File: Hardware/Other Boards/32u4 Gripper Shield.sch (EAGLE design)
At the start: 22 parts, among them Q1 MOSFET-NCHANNELSMD, Q2 MOSFET-NCHANNELSMD, U1 SN74LS241DW, U2 XBEE-1B3, U3 V_REG_LDOSMD

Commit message: Few more things with shield
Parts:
- Q1, Q2: value MOSFET-NCHANNELSMD -> MOSFET-NCHANNELBSS138; device SparkFun-DiscreteSemi:MOSFET-NCHANNELSMD -> SparkFun-DiscreteSemi:MOSFET-NCHANNELBSS138
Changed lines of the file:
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@@
 <part name="P+3" library="SparkFun" deviceset="3.3V" device=""/>
 <part name="P+4" library="SparkFun" deviceset="3.3V" device=""/>
-<part name="Q1" library="SparkFun-DiscreteSemi" deviceset="MOSFET-NCHANNEL" device="SMD"/>
+<part name="Q1" library="SparkFun-DiscreteSemi" deviceset="MOSFET-NCHANNEL" device="BSS138"/>
 <part name="R5" library="SparkFun-Passives" deviceset="RESISTOR" device="1206" value="1k"/>
 <part name="R6" library="SparkFun-Passives" deviceset="RESISTOR" device="1206" value="1k"/>
 <part name="P+5" library="SparkFun" deviceset="3.3V" device=""/>
 <part name="U$6" library="SparkFun" deviceset="5V" device=""/>
-<part name="Q2" library="SparkFun-DiscreteSemi" deviceset="MOSFET-NCHANNEL" device="SMD"/>
+<part name="Q2" library="SparkFun-DiscreteSemi" deviceset="MOSFET-NCHANNEL" device="BSS138"/>
 <part name="R7" library="SparkFun-Passives" deviceset="RESISTOR" device="1206" value="1k"/>
 <part name="R8" library="SparkFun-Passives" deviceset="RESISTOR" device="1206" value="1k"/>
@@
 <pinref part="JP1" gate="G$1" pin="3"/>
 <wire x1="63.5" y1="106.68" x2="73.66" y2="106.68" width="0.1524" layer="91"/>
+<label x="73.66" y="106.68" size="1.778" layer="95"/>
 </segment>
 <segment>
@@
 <pinref part="U$5" gate="G$1" pin="OUT"/>
 <wire x1="167.64" y1="142.24" x2="172.72" y2="142.24" width="0.1524" layer="91"/>
+<label x="172.72" y="142.24" size="1.778" layer="95" xref="yes"/>
 </segment>
 </net>
@@
 <pinref part="JP1" gate="G$1" pin="1"/>
 <wire x1="63.5" y1="101.6" x2="73.66" y2="101.6" width="0.1524" layer="91"/>
+<label x="73.66" y="101.6" size="1.778" layer="95"/>
 </segment>
 </net>
@@
 <pinref part="U$1" gate="G$1" pin="D3~"/>
 <wire x1="5.08" y1="55.88" x2="-2.54" y2="55.88" width="0.1524" layer="91"/>
+<label x="-5.08" y="55.88" size="1.778" layer="95"/>
 </segment>
 </net>
@@
 <pinref part="U$1" gate="G$1" pin="D2"/>
 <wire x1="5.08" y1="60.96" x2="-2.54" y2="60.96" width="0.1524" layer="91"/>
+<label x="-5.08" y="60.96" size="1.778" layer="95"/>
 </segment>
 </net>
@@
 <pinref part="JP1" gate="G$1" pin="2"/>
 <wire x1="63.5" y1="104.14" x2="73.66" y2="104.14" width="0.1524" layer="91"/>
+<label x="73.66" y="104.14" size="1.778" layer="95"/>
 </segment>
 <segment>
 <pinref part="U$5" gate="G$1" pin="IN"/>
 <wire x1="152.4" y1="142.24" x2="147.32" y2="142.24" width="0.1524" layer="91"/>
+<label x="147.32" y="142.24" size="1.778" layer="95" rot="R180" xref="yes"/>
 </segment>
 <segment>
 <pinref part="U$3" gate="G$1" pin="L"/>
 <wire x1="154.94" y1="162.56" x2="149.86" y2="162.56" width="0.1524" layer="91"/>
+<label x="149.86" y="162.56" size="1.778" layer="95" rot="R180" xref="yes"/>
 </segment>
 </net>
@@
 <pinref part="U$1" gate="G$1" pin="D1/TX"/>
 <wire x1="5.08" y1="71.12" x2="-2.54" y2="71.12" width="0.1524" layer="91"/>
+<label x="-5.08" y="71.12" size="1.778" layer="95"/>
 </segment>
 <segment>
@@
 <pinref part="U$1" gate="G$1" pin="D0/RX"/>
 <wire x1="5.08" y1="66.04" x2="-2.54" y2="66.04" width="0.1524" layer="91"/>
-</segment>
-<segment>
+<label x="-5.08" y="66.04" size="1.778" layer="95"/>
+</segment>
+<segment>

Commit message: Finished gripper shield
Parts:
- removed C1, C3: 10uF, SparkFun:CAP_POL1206
- removed C2: 0.1uF, SparkFun-Passives:CAP1206
- removed Q1, Q2: MOSFET-NCHANNELBSS138, SparkFun-DiscreteSemi:MOSFET-NCHANNELBSS138
- removed R5, R6, R7, R8: 1k, SparkFun-Passives:RESISTOR1206
- removed U3: V_REG_LDOSMD, SparkFun:V_REG_LDOSMD
- added S1, S2, S3, S4: STANDOFF_ELECTRICAL, SparkFun-Electromechanical:STANDOFF_ELECTRICAL
- U$3: value H_WR-TBL_3210002HORIZ -> H_WR-TBL_321*0002VERT; device MRDT-2015-PowerBoard:H_WR-TBL_3210002HORIZ -> MRDT-2015-PowerBoard:H_WR-TBL_3210002VERT
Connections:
- removed net 5V: C3.+, R6.2, R8.2, U$1.VCC, U$5.OUT, U1.VCC, U3.EN, U3.IN
- removed net DIN: Q1.D, R6.1
- removed net DOUT: Q2.D, R8.1
- net 3.3V: now also U$1.VCC, U$5.OUT, U1.VCC; no longer C1.+, C2.1, Q1.G, Q2.G, R5.2, R7.2, U3.OUT
- net DC_1: now also U$1.D4/A6
- net GND: now also S1.P$1, S2.P$1, S3.P$1, S4.P$1; no longer C1.-, C2.2, C3.-, U3.GND
- net RX_0: no longer Q2.S, R7.1
- net TX_0: no longer Q1.S, R5.1
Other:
- note removed: "500mA peak"
- note removed: "MIC5219-3.3V"

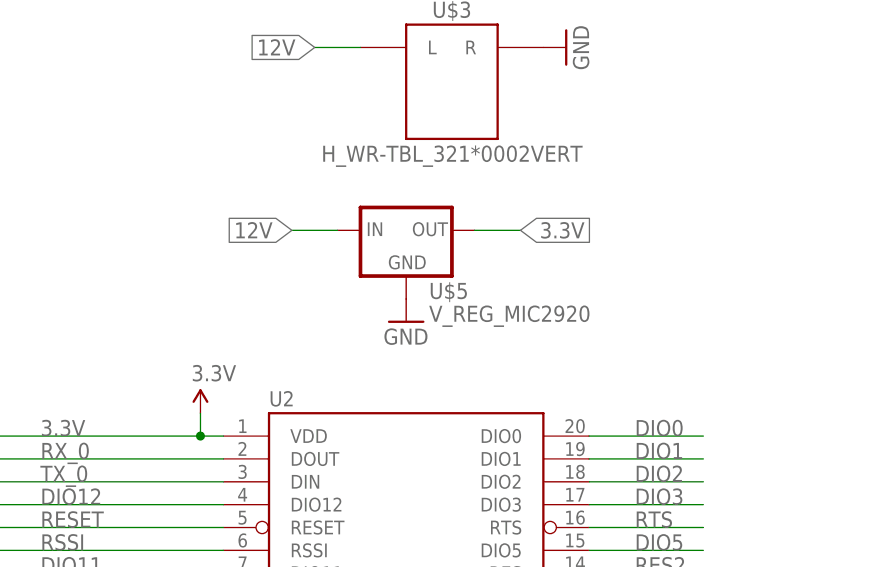
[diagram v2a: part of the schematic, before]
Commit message: Finished shields for aux
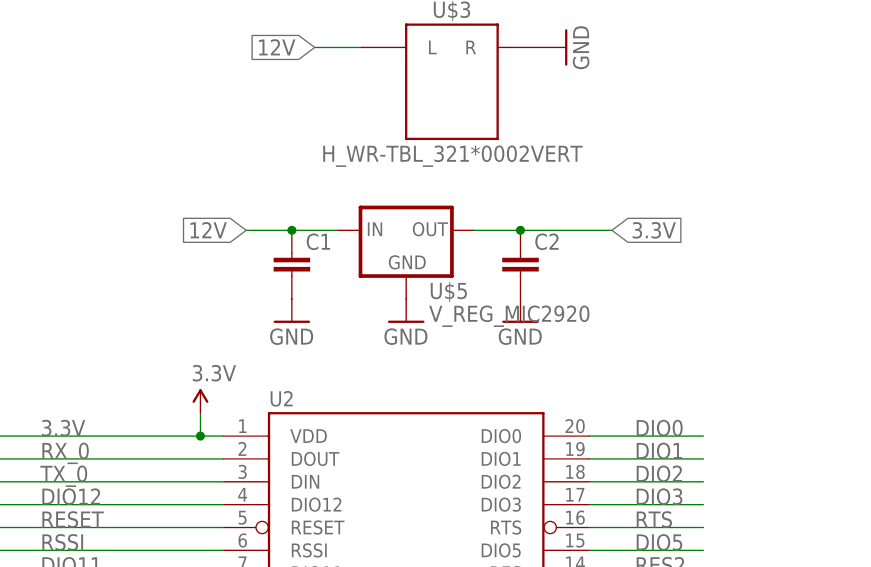
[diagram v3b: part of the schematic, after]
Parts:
- added C1, C2: (no value), SparkFun-Passives:CAP1206
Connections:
- net 12V: now also C1.1
- net 3.3V: now also C2.1
- net GND: now also C1.2, C2.2
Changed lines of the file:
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@@
 <part name="GND7" library="SparkFun" deviceset="GND" device=""/>
 <part name="GND8" library="SparkFun" deviceset="GND" device=""/>
+<part name="C1" library="SparkFun-Passives" deviceset="CAP" device="1206"/>
+<part name="C2" library="SparkFun-Passives" deviceset="CAP" device="1206"/>
+<part name="GND10" library="SparkFun" deviceset="GND" device=""/>
+<part name="GND11" library="SparkFun" deviceset="GND" device=""/>
 </parts>
 <sheets>
@@
 <instance part="GND7" gate="1" x="111.76" y="45.72" rot="R90"/>
 <instance part="GND8" gate="1" x="111.76" y="33.02" rot="R90"/>
+<instance part="C1" gate="G$1" x="147.32" y="137.16"/>
+<instance part="C2" gate="G$1" x="172.72" y="137.16"/>
+<instance part="GND10" gate="1" x="147.32" y="132.08"/>
+<instance part="GND11" gate="1" x="172.72" y="132.08"/>
 </instances>
 <busses>
@@
 <pinref part="GND8" gate="1" pin="GND"/>
 </segment>
+<segment>
+<pinref part="C1" gate="G$1" pin="2"/>
+<pinref part="GND10" gate="1" pin="GND"/>
+</segment>
+<segment>
+<pinref part="C2" gate="G$1" pin="2"/>
+<pinref part="GND11" gate="1" pin="GND"/>
+</segment>
 </net>
 <net name="RESET" class="0">
@@
 <pinref part="U$5" gate="G$1" pin="OUT"/>
 <wire x1="167.64" y1="142.24" x2="172.72" y2="142.24" width="0.1524" layer="91"/>
-<label x="172.72" y="142.24" size="1.778" layer="95" xref="yes"/>
+<label x="182.88" y="142.24" size="1.778" layer="95" xref="yes"/>
+<pinref part="C2" gate="G$1" pin="1"/>
+<wire x1="172.72" y1="142.24" x2="182.88" y2="142.24" width="0.1524" layer="91"/>
+<junction x="172.72" y="142.24"/>
 </segment>
 </net>
@@
 <pinref part="U$5" gate="G$1" pin="IN"/>
 <wire x1="152.4" y1="142.24" x2="147.32" y2="142.24" width="0.1524" layer="91"/>
-<label x="147.32" y="142.24" size="1.778" layer="95" rot="R180" xref="yes"/>
-</segment>
-<segment>
+<label x="142.24" y="142.24" size="1.778" layer="95" rot="R180" xref="yes"/>
+<pinref part="C1" gate="G$1" pin="1"/>
+<wire x1="147.32" y1="142.24" x2="142.24" y2="142.24" width="0.1524" layer="91"/>
+<junction x="147.32" y="142.24"/>
+</segment>
+<segment>
